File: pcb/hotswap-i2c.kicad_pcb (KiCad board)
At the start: 2 copper layers, 17.2 x 11.2 mm, 6 parts, among them J1 Conn_01x04_Male, J2 Conn_01x02_Male, U1 TCA4311ADR

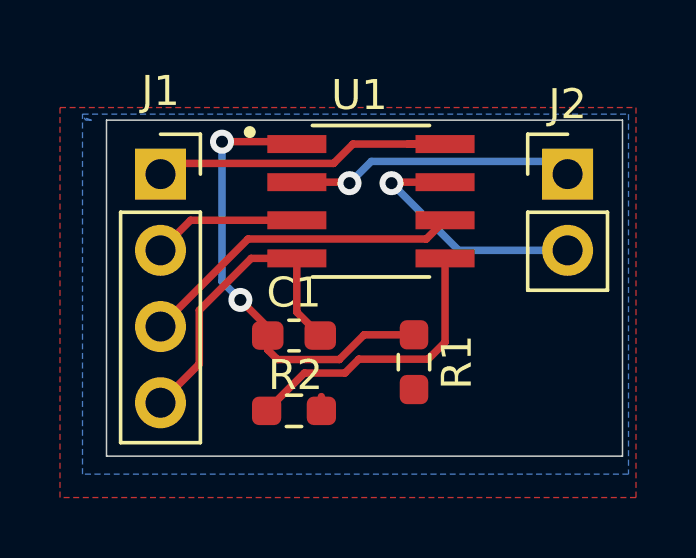
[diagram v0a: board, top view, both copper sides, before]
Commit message: add decoupling cap
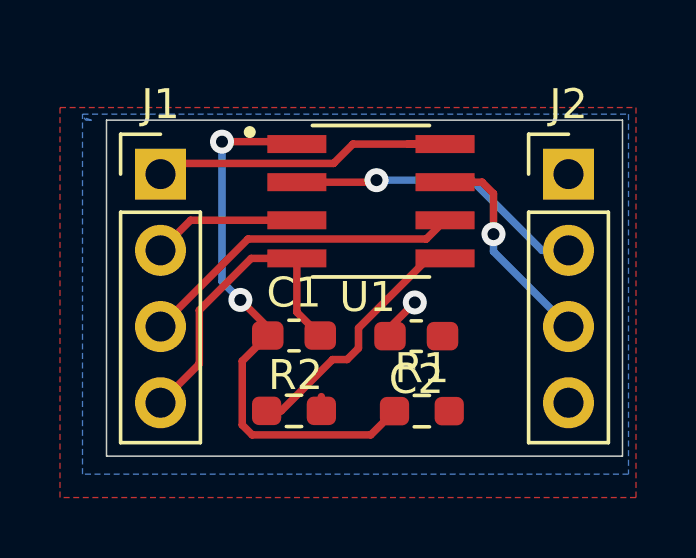
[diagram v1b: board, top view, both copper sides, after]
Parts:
- added C2: 0.01uF, Capacitor_SMD:C_0603_1608Metric_Pad1.05x0.95mm_HandSolder, F.Cu at (149.8, 84.2)
- J1: footprint Connector_PinSocket_2.54mm:PinSocket_1x04_P2.54mm_Vertical -> Connector_PinHeader_2.54mm:PinHeader_1x04_P2.54mm_Vertical
- J2: value Conn_01x02_Male -> Conn_01x04_Male; footprint Connector_PinHeader_2.54mm:PinHeader_1x02_P2.54mm_Vertical -> Connector_PinHeader_2.54mm:PinHeader_1x04_P2.54mm_Vertical
- moved R1 1.65 mm to (150.0, 86.7), turned to 0 degrees
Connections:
- J2 pad 1: SCLOUT -> VCC
- J2 pad 2: SDAOUT -> SCLOUT
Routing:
- net Net-(C1-Pad1): track 15.4 -> 18.5 mm
- net GND: track 10.5 -> 11.9 mm, vias 0 -> 1
- net SDAOUT: track 8.60 -> 7.24 mm
- net Net-(R2-Pad2): track 9.69 -> 8.45 mm
- net SCLOUT: track 9.51 -> 10.1 mm
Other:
- board text added: "GND"
- board text added: "SCLIN"
- board text added: "SCLOUT"
- board text added: "SDAIN"
- board text added: "SDAOUT"
- board text added: "VCC"

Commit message: some rerouting
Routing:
- net SDAOUT: track 7.24 -> 10.7 mm
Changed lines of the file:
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@@
     (tags "capacitor handsolder")
     (attr smd)
-    (fp_text reference C2 (at 0 -1.43) (layer F.SilkS)
+    (fp_text reference C2 (at -0.175 -1.4) (layer F.SilkS)
       (effects (font (size 1 1) (thickness 0.15)))
     )
     (fp_text value 0.01uF (at 0 1.43) (layer F.Fab)
       (effects (font (size 1 1) (thickness 0.15)))
-    )
-    (fp_text user %R (at 0 0) (layer F.Fab)
-      (effects (font (size 0.4 0.4) (thickness 0.06)))
     )
     (fp_line (start -0.8 0.4) (end -0.8 -0.4) (layer F.Fab) (width 0.1))
@@
     (fp_line (start 1.65 -0.73) (end 1.65 0.73) (layer F.CrtYd) (width 0.05))
     (fp_line (start 1.65 0.73) (end -1.65 0.73) (layer F.CrtYd) (width 0.05))
+    (fp_text user %R (at 0 0) (layer F.Fab)
+      (effects (font (size 0.4 0.4) (thickness 0.06)))
+    )
     (pad 2 smd roundrect (at 0.875 0 180) (size 1.05 0.95) (layers F.Cu F.Paste F.Mask) (roundrect_rratio 0.25)
       (net 1 GND))
@@
     (tags "resistor handsolder")
     (attr smd)
-    (fp_text reference R1 (at 0 -1.43) (layer F.SilkS)
+    (fp_text reference R1 (at 2.4875 -2.5) (layer F.SilkS)
       (effects (font (size 1 1) (thickness 0.15)))
     )
@@
   (segment (start 142.2525 80.3575) (end 145.795 80.3575) (width 0.25) (layer F.Cu) (net 3))
   (segment (start 141.25 81.36) (end 142.2525 80.3575) (width 0.25) (layer F.Cu) (net 3))
-  (via (at 152.35 80.82) (size 0.8) (drill 0.4) (layers F.Cu B.Cu) (net 4))
-  (segment (start 152.35 79.4675) (end 152.35 80.82) (width 0.25) (layer F.Cu) (net 4))
-  (segment (start 151.97 79.0875) (end 152.35 79.4675) (width 0.25) (layer F.Cu) (net 4))
-  (segment (start 150.735 79.0875) (end 151.97 79.0875) (width 0.25) (layer F.Cu) (net 4))
-  (segment (start 152.35 81.4) (end 154.85 83.9) (width 0.25) (layer B.Cu) (net 4))
-  (segment (start 152.35 80.82) (end 152.35 81.4) (width 0.25) (layer B.Cu) (net 4))
+  (via (at 148.45 80.020003) (size 0.8) (drill 0.4) (layers F.Cu B.Cu) (net 4))
+  (segment (start 148.522999 80.020003) (end 148.45 80.020003) (width 0.25) (layer F.Cu) (net 4))
+  (segment (start 149.455502 79.0875) (end 148.522999 80.020003) (width 0.25) (layer F.Cu) (net 4))
+  (segment (start 150.735 79.0875) (end 149.455502 79.0875) (width 0.25) (layer F.Cu) (net 4))
+  (segment (start 150.970003 80.020003) (end 154.85 83.9) (width 0.25) (layer B.Cu) (net 4))
+  (segment (start 148.45 80.020003) (end 150.970003 80.020003) (width 0.25) (layer B.Cu) (net 4))
   (via (at 148.45 79.02) (size 0.8) (drill 0.4) (layers F.Cu B.Cu) (net 5))
   (segment (start 148.3825 79.0875) (end 148.45 79.02) (width 0.25) (layer F.Cu) (net 5))

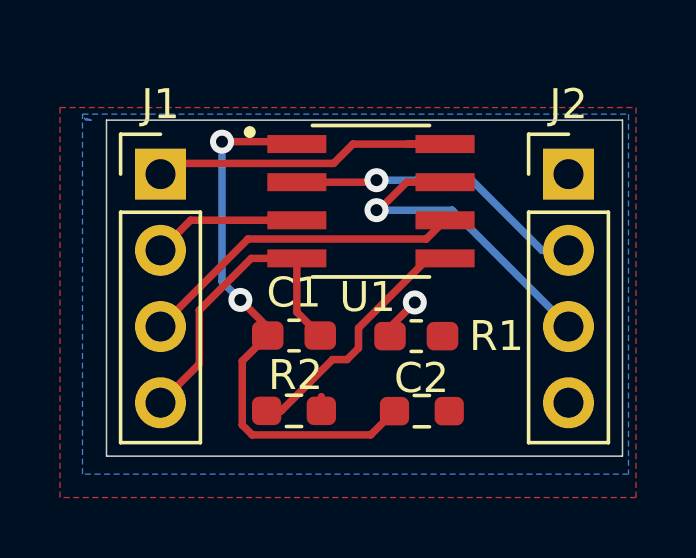
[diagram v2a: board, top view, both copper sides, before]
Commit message: update design, add license
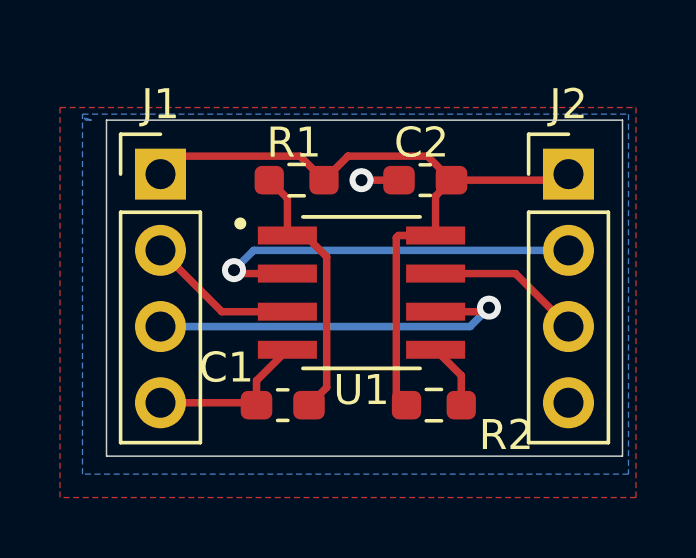
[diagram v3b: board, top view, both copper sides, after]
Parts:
- moved R1 8.76 mm to (145.8, 79.0)
- moved C2 5.21 mm to (150.1, 79.0)
- moved R2 4.67 mm to (150.4, 86.5), turned to 0 degrees
- moved U1 3.06 mm to (147.9, 82.8)
- moved C1 2.35 mm to (145.3, 86.5), turned to 180 degrees
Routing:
- net VCC: track 11.6 -> 24.1 mm
- net Net-(C1-Pad1): track 18.5 -> 8.89 mm, vias 2 -> 0
- net Net-(R2-Pad2): track 8.45 -> 2.20 mm
- net SDAOUT: track 10.7 -> 5.16 mm, vias 1 -> 0
- net GND: track 11.9 -> 6.75 mm
- net SCLOUT: track 10.1 -> 13.3 mm
- net SDAIN: track 11.0 -> 13.0 mm, vias 0 -> 1

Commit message: update image
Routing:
- net VCC: track 24.1 -> 0.48 mm
